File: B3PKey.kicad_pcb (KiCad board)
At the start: 2 copper layers, 178 parts, among them SW1 SW_Push, U1 ATmega32U4-AU, Y1 16MHz

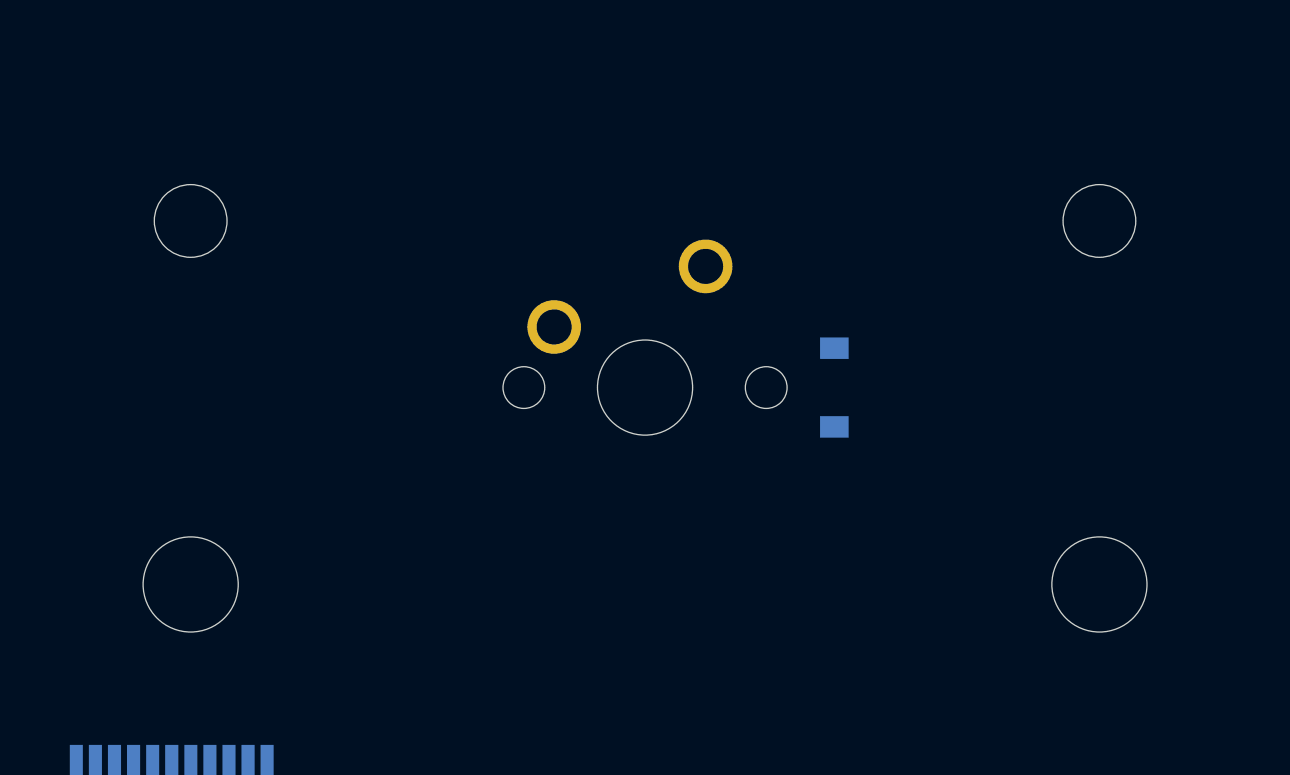
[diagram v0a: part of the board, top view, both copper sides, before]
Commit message: Flip spacebar stabs
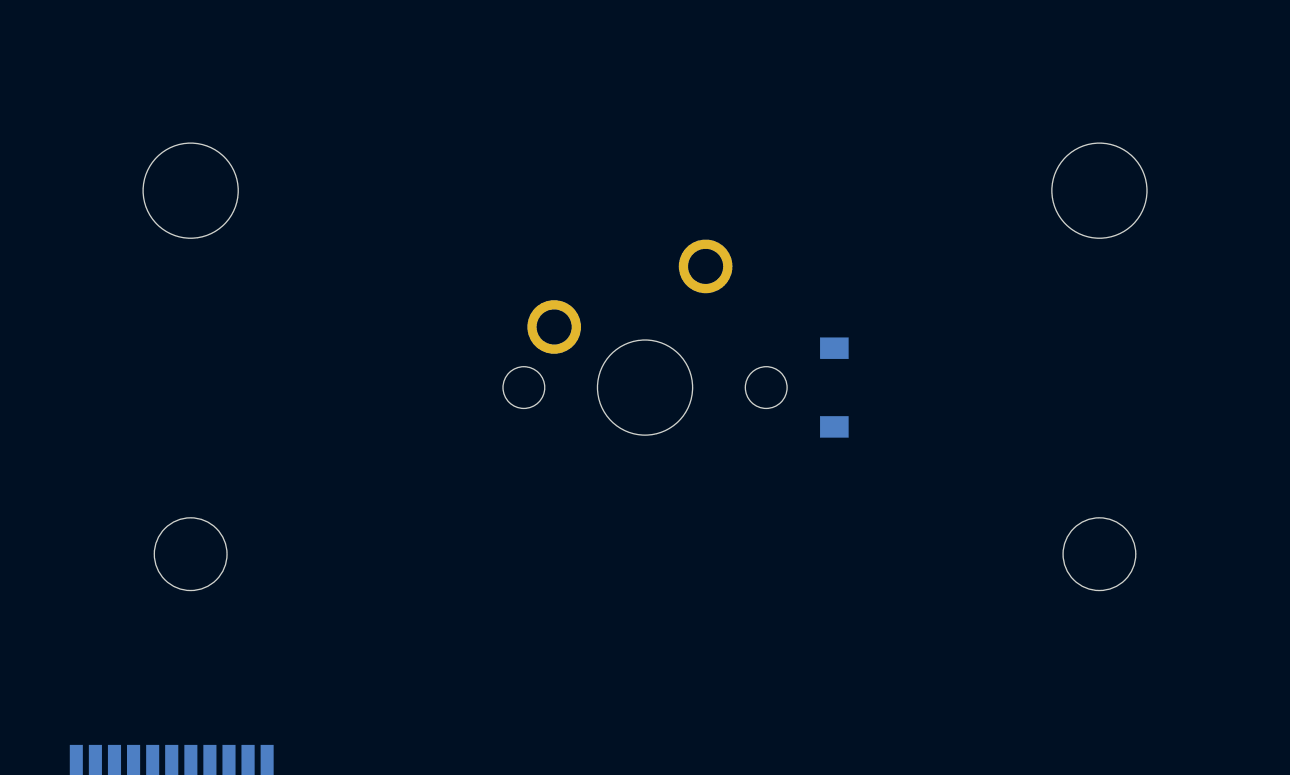
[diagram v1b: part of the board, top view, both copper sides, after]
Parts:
- MX74: footprint MX_Only:MXOnly-3U-NoLED -> MX_Only:MXOnly-3U-ReversedStabilizers-NoLED
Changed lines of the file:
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@@
     (add_net VCC)
+  )
+  (module MX_Only:MXOnly-3U-ReversedStabilizers-NoLED (layer F.Cu)
+    (at 117.475 117.475)
+    (fp_text reference MX74 (at 0 3.175) (layer Dwgs.User)
+      (effects (font (size 1 1) (thickness 0.15)))
+    )
+    (fp_text value MX-NoLED (at 0 -7.9375) (layer Dwgs.User)
+      (effects (font (size 1 1) (thickness 0.15)))
+    )
+    (fp_line (start 5 -7) (end 7 -7) (layer Dwgs.User) (width 0.15))
+    (fp_line (start 7 -7) (end 7 -5) (layer Dwgs.User) (width 0.15))
+    (fp_line (start 5 7) (end 7 7) (layer Dwgs.User) (width 0.15))
+    (fp_line (start 7 7) (end 7 5) (layer Dwgs.User) (width 0.15))
+    (fp_line (start -7 5) (end -7 7) (layer Dwgs.User) (width 0.15))
+    (fp_line (start -7 7) (end -5 7) (layer Dwgs.User) (width 0.15))
+    (fp_line (start -5 -7) (end -7 -7) (layer Dwgs.User) (width 0.15))
+    (fp_line (start -7 -7) (end -7 -5) (layer Dwgs.User) (width 0.15))
+    (fp_line (start -28.575 -9.525) (end 28.575 -9.525) (layer Dwgs.User) (width 0.15))
+    (fp_line (start 28.575 -9.525) (end 28.575 9.525) (layer Dwgs.User) (width 0.15))
+    (fp_line (start -28.575 9.525) (end 28.575 9.525) (layer Dwgs.User) (width 0.15))
+    (fp_line (start -28.575 9.525) (end -28.575 -9.525) (layer Dwgs.User) (width 0.15))
+    (pad 2 thru_hole circle (at 2.54 -5.08) (size 2.25 2.25) (drill 1.47) (layers *.Cu B.Mask)
+      (net 85 "Net-(D74-Pad2)"))
+    (pad 1 thru_hole circle (at -3.81 -2.54 48.1) (size 2.25 2.25) (drill 1.47) (layers *.Cu B.Mask)
+      (net 98 COL5))
+    (pad "" np_thru_hole circle (at 0 0) (size 3.9878 3.9878) (drill 3.9878) (layers *.Cu *.Mask))
+    (pad "" np_thru_hole circle (at -5.08 0 48.0996) (size 1.75 1.75) (drill 1.75) (layers *.Cu *.Mask))
+    (pad "" np_thru_hole circle (at 5.08 0 48.0996) (size 1.75 1.75) (drill 1.75) (layers *.Cu *.Mask))
+    (pad "" np_thru_hole circle (at -19.05 6.985) (size 3.048 3.048) (drill 3.048) (layers *.Cu *.Mask))
+    (pad "" np_thru_hole circle (at 19.05 6.985) (size 3.048 3.048) (drill 3.048) (layers *.Cu *.Mask))
+    (pad "" np_thru_hole circle (at -19.05 -8.255) (size 3.9878 3.9878) (drill 3.9878) (layers *.Cu *.Mask))
+    (pad "" np_thru_hole circle (at 19.05 -8.255) (size 3.9878 3.9878) (drill 3.9878) (layers *.Cu *.Mask))
   )
   (module MX_Only:MXOnly-1U-NoLED (layer F.Cu)
@@
     (pad "" np_thru_hole circle (at 5.08 0 48.0996) (size 1.75 1.75) (drill 1.75) (layers *.Cu *.Mask))
   )
-  (module MX_Only:MXOnly-3U-NoLED (layer F.Cu)
-    (at 117.475 117.475)
-    (fp_text reference MX74 (at 0 3.175) (layer Dwgs.User)
-      (effects (font (size 1 1) (thickness 0.15)))
-    )
-    (fp_text value MX-NoLED (at 0 -7.9375) (layer Dwgs.User)
-      (effects (font (size 1 1) (thickness 0.15)))
-    )
-    (fp_line (start 5 -7) (end 7 -7) (layer Dwgs.User) (width 0.15))
-    (fp_line (start 7 -7) (end 7 -5) (layer Dwgs.User) (width 0.15))
-    (fp_line (start 5 7) (end 7 7) (layer Dwgs.User) (width 0.15))
-    (fp_line (start 7 7) (end 7 5) (layer Dwgs.User) (width 0.15))
-    (fp_line (start -7 5) (end -7 7) (layer Dwgs.User) (width 0.15))
-    (fp_line (start -7 7) (end -5 7) (layer Dwgs.User) (width 0.15))
-    (fp_line (start -5 -7) (end -7 -7) (layer Dwgs.User) (width 0.15))
-    (fp_line (start -7 -7) (end -7 -5) (layer Dwgs.User) (width 0.15))
-    (fp_line (start -28.575 -9.525) (end 28.575 -9.525) (layer Dwgs.User) (width 0.15))
-    (fp_line (start 28.575 -9.525) (end 28.575 9.525) (layer Dwgs.User) (width 0.15))
-    (fp_line (start -28.575 9.525) (end 28.575 9.525) (layer Dwgs.User) (width 0.15))
-    (fp_line (start -28.575 9.525) (end -28.575 -9.525) (layer Dwgs.User) (width 0.15))
-    (pad 2 thru_hole circle (at 2.54 -5.08) (size 2.25 2.25) (drill 1.47) (layers *.Cu B.Mask)
-      (net 85 "Net-(D74-Pad2)"))
-    (pad 1 thru_hole circle (at -3.81 -2.54 48.1) (size 2.25 2.25) (drill 1.47) (layers *.Cu B.Mask)
-      (net 98 COL5))
-    (pad "" np_thru_hole circle (at 0 0) (size 3.9878 3.9878) (drill 3.9878) (layers *.Cu *.Mask))
-    (pad "" np_thru_hole circle (at -5.08 0 48.0996) (size 1.75 1.75) (drill 1.75) (layers *.Cu *.Mask))
-    (pad "" np_thru_hole circle (at 5.08 0 48.0996) (size 1.75 1.75) (drill 1.75) (layers *.Cu *.Mask))
-    (pad "" np_thru_hole circle (at -19.05 -6.985) (size 3.048 3.048) (drill 3.048) (layers *.Cu *.Mask))
-    (pad "" np_thru_hole circle (at 19.05 -6.985) (size 3.048 3.048) (drill 3.048) (layers *.Cu *.Mask))
-    (pad "" np_thru_hole circle (at -19.05 8.255) (size 3.9878 3.9878) (drill 3.9878) (layers *.Cu *.Mask))
-    (pad "" np_thru_hole circle (at 19.05 8.255) (size 3.9878 3.9878) (drill 3.9878) (layers *.Cu *.Mask))
-  )
-  (module MX_Only:MXOnly-1U-NoLED (layer F.Cu)
+  (module MX_Only:MXOnly-1U-NoLED (layer F.Cu)

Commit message: Matrix traces laid
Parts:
- moved D55 6.74 mm to (263.5, 84.1)
- moved D21 6.74 mm to (139.7, 46.0)
- moved D24 6.74 mm to (196.8, 46.0)
- moved D26 6.74 mm to (234.9, 46.0)
- moved D35 6.74 mm to (139.7, 65.1)
- moved D38 6.74 mm to (196.8, 65.1)
- moved D40 6.74 mm to (234.9, 65.1)
- moved D49 6.74 mm to (139.7, 84.1)
- moved D52 6.74 mm to (196.8, 84.1)
- moved D54 6.74 mm to (234.9, 84.1)
- moved D62 6.74 mm to (139.7, 103.2)
- moved D65 6.74 mm to (196.8, 103.2)
- moved D67 6.74 mm to (234.9, 103.2)
- moved D77 6.74 mm to (196.8, 122.2)
- moved D79 6.74 mm to (234.9, 122.2)
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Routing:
- net ROW5: track 0.00 -> 251.0 mm
- net ROW4: track 0.00 -> 247.7 mm
- net ROW2: track 0.00 -> 247.7 mm
- net ROW1: track 0.00 -> 247.7 mm
- net ROW0: track 0.00 -> 247.7 mm
- net ROW3: track 0.00 -> 239.0 mm
- net COL12: track 0.00 -> 105.3 mm
- net COL13: track 0.00 -> 96.3 mm
- net COL0: track 0.00 -> 95.3 mm
- net COL9: track 0.00 -> 95.2 mm
- net COL8: track 0.00 -> 95.2 mm
- net COL7: track 0.00 -> 95.2 mm
- net COL5: track 0.00 -> 95.2 mm
- net COL3: track 0.00 -> 95.2 mm
- net COL2: track 0.00 -> 95.2 mm
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
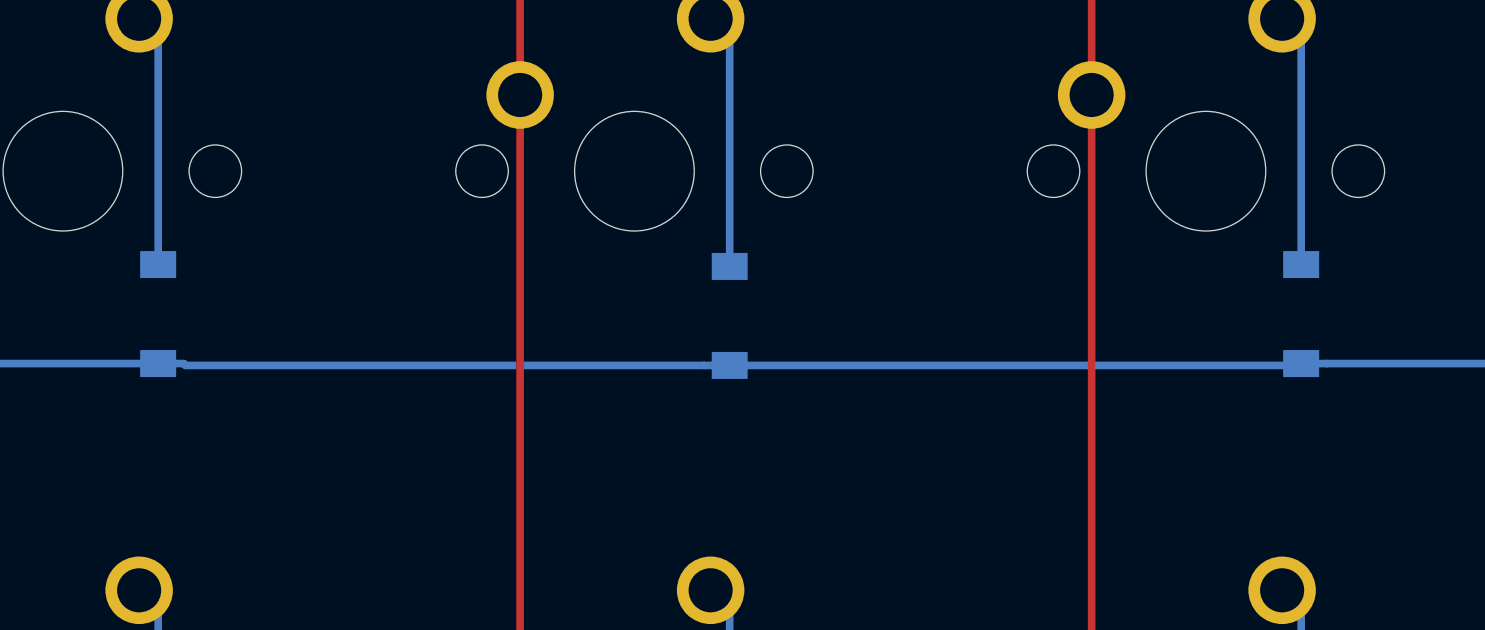
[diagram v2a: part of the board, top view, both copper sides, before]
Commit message: Matrix traces tweak
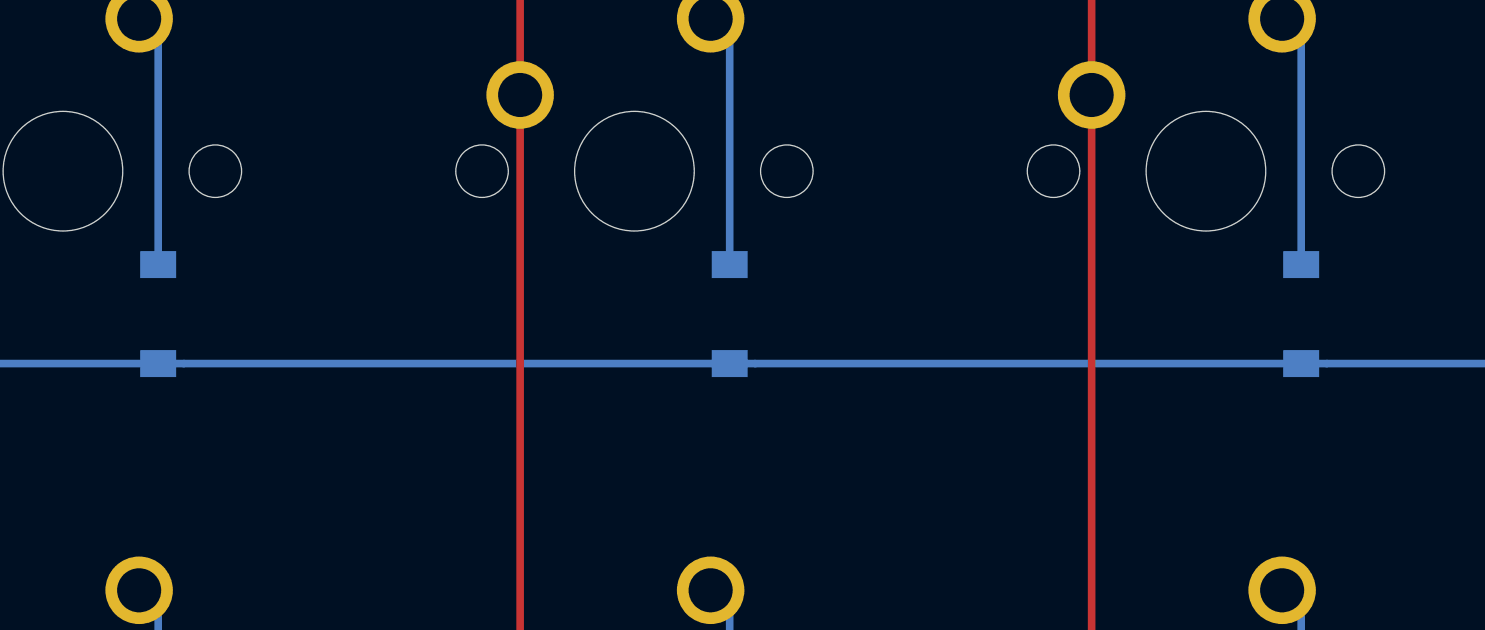
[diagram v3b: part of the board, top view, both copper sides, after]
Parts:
- moved D50 0.06 mm to (158.8, 84.1)
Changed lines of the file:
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@@
     (thickness 1.6)
     (drawings 0)
-    (tracks 366)
+    (tracks 365)
     (zones 0)
     (modules 178)
@@
   )
   (module Diode_SMD:D_SOD-123 (layer B.Cu)
-    (at 158.75 84.2 90)
+    (at 158.75 84.1375 90)
     (descr SOD-123)
     (tags SOD-123)
@@
   (segment (start 273.05 55.88) (end 272.415 55.245) (width 0.254) (layer B.Cu) (net 50))
   (segment (start 273.05 63.4375) (end 273.05 55.88) (width 0.254) (layer B.Cu) (net 50))
-  (segment (start 26.254 85.7875) (end 44.45 85.7875) (width 0.254) (layer B.Cu) (net 51))
-  (segment (start 25.4 85.7875) (end 26.254 85.7875) (width 0.254) (layer B.Cu) (net 51))
-  (segment (start 45.304 85.7875) (end 63.5 85.7875) (width 0.254) (layer B.Cu) (net 51))
-  (segment (start 44.45 85.7875) (end 45.304 85.7875) (width 0.254) (layer B.Cu) (net 51))
-  (segment (start 64.354 85.7875) (end 82.55 85.7875) (width 0.254) (layer B.Cu) (net 51))
-  (segment (start 63.5 85.7875) (end 64.354 85.7875) (width 0.254) (layer B.Cu) (net 51))
-  (segment (start 83.404 85.7875) (end 101.6 85.7875) (width 0.254) (layer B.Cu) (net 51))
-  (segment (start 82.55 85.7875) (end 83.404 85.7875) (width 0.254) (layer B.Cu) (net 51))
-  (segment (start 102.454 85.7875) (end 120.65 85.7875) (width 0.254) (layer B.Cu) (net 51))
-  (segment (start 101.6 85.7875) (end 102.454 85.7875) (width 0.254) (layer B.Cu) (net 51))
-  (segment (start 121.504 85.7875) (end 139.7 85.7875) (width 0.254) (layer B.Cu) (net 51))
-  (segment (start 120.65 85.7875) (end 121.504 85.7875) (width 0.254) (layer B.Cu) (net 51))
-  (segment (start 157.896 85.85) (end 158.75 85.85) (width 0.254) (layer B.Cu) (net 51))
-  (segment (start 140.6165 85.85) (end 157.896 85.85) (width 0.254) (layer B.Cu) (net 51))
-  (segment (start 140.554 85.7875) (end 140.6165 85.85) (width 0.254) (layer B.Cu) (net 51))
-  (segment (start 139.7 85.7875) (end 140.554 85.7875) (width 0.254) (layer B.Cu) (net 51))
   (segment (start 177.7375 85.85) (end 177.8 85.7875) (width 0.254) (layer B.Cu) (net 51))
-  (segment (start 158.75 85.85) (end 177.7375 85.85) (width 0.254) (layer B.Cu) (net 51))
   (segment (start 178.654 85.7875) (end 196.85 85.7875) (width 0.254) (layer B.Cu) (net 51))
   (segment (start 177.8 85.7875) (end 178.654 85.7875) (width 0.254) (layer B.Cu) (net 51))
@@
   (segment (start 236.7555 84.836) (end 235.804 85.7875) (width 0.254) (layer B.Cu) (net 51))
   (segment (start 261.7195 84.836) (end 236.7555 84.836) (width 0.254) (layer B.Cu) (net 51))
+  (segment (start 120.65 85.7875) (end 121.504 85.7875) (width 0.254) (layer B.Cu) (net 51))
+  (segment (start 102.454 85.7875) (end 120.65 85.7875) (width 0.254) (layer B.Cu) (net 51))
+  (segment (start 63.5 85.7875) (end 64.354 85.7875) (width 0.254) (layer B.Cu) (net 51))
+  (segment (start 64.354 85.7875) (end 82.55 85.7875) (width 0.254) (layer B.Cu) (net 51))
+  (segment (start 26.254 85.7875) (end 44.45 85.7875) (width 0.254) (layer B.Cu) (net 51))
+  (segment (start 44.45 85.7875) (end 45.304 85.7875) (width 0.254) (layer B.Cu) (net 51))
+  (segment (start 25.4 85.7875) (end 26.254 85.7875) (width 0.254) (layer B.Cu) (net 51))
+  (segment (start 121.504 85.7875) (end 139.7 85.7875) (width 0.254) (layer B.Cu) (net 51))
+  (segment (start 82.55 85.7875) (end 83.404 85.7875) (width 0.254) (layer B.Cu) (net 51))
+  (segment (start 83.404 85.7875) (end 101.6 85.7875) (width 0.254) (layer B.Cu) (net 51))
+  (segment (start 101.6 85.7875) (end 102.454 85.7875) (width 0.254) (layer B.Cu) (net 51))
+  (segment (start 45.304 85.7875) (end 63.5 85.7875) (width 0.254) (layer B.Cu) (net 51))
+  (segment (start 140.554 85.7875) (end 158.75 85.7875) (width 0.254) (layer B.Cu) (net 51))
+  (segment (start 139.7 85.7875) (end 140.554 85.7875) (width 0.254) (layer B.Cu) (net 51))
+  (segment (start 159.604 85.7875) (end 177.8 85.7875) (width 0.254) (layer B.Cu) (net 51))
+  (segment (start 158.75 85.7875) (end 159.604 85.7875) (width 0.254) (layer B.Cu) (net 51))
   (segment (start 25.4 74.93) (end 24.765 74.295) (width 0.254) (layer B.Cu) (net 52))
   (segment (start 25.4 82.4875) (end 25.4 74.93) (width 0.254) (layer B.Cu) (net 52))

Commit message: Add Elite-C footprint
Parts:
- added U1: Elite-C, Keebio-Parts:Elite-C, F.Cu at (60.3, 30.7)
- moved D17 3.24 mm to (63.5, 49.3)
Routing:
- net Net-(D17-Pad2): track 8.46 -> 13.1 mm
- net ROW1: track 247.7 -> 250.3 mm
- net ROW0: track 247.7 -> 248.3 mm

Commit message: Update layout and replace microcontroller
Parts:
- removed C1, C2: 22pF, Capacitor_SMD:C_0805_2012Metric
- removed C3: 1uF, Capacitor_SMD:C_0805_2012Metric
- removed C4, C5, C6: 0.1uF, Capacitor_SMD:C_0805_2012Metric
- removed C7: 10uF, Capacitor_SMD:C_0805_2012Metric
- removed F1: 500mA, Fuse:Fuse_0805_2012Metric
- removed R1, R4: 10k, Resistor_SMD:R_0805_2012Metric
- removed R2, R3: 22, Resistor_SMD:R_0805_2012Metric
- removed SW1: SW_Push, random-keyboard-parts:SKQG-1155865
- removed U1: ATmega32U4-AU, Package_QFP:TQFP-44_10x10mm_P0.8mm
- removed U1: Elite-C, Keebio-Parts:Elite-C
- removed USB1: Molex-0548190589, random-keyboard-parts:Molex-0548190589
- removed Y1: 16MHz, Crystal:Crystal_SMD_3225-4Pin_3.2x2.5mm
- added U2: Elite-C, Keebio-Parts:Elite-C, F.Cu at (60.3, 30.7)
- MX74: footprint MX_Only:MXOnly-3U-ReversedStabilizers-NoLED -> MX_Only:MXOnly-2U-ReversedStabilizers-NoLED
- MX75: footprint MX_Only:MXOnly-1U-NoLED -> MX_Only:MXOnly-2U-ReversedStabilizers-NoLED
- moved D74 9.53 mm to (111.1, 122.2)
- moved D75 9.53 mm to (149.2, 122.2)
- moved MX74 9.52 mm to (108.0, 117.5)
- moved MX75 9.52 mm to (146.1, 117.5)
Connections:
- MX75 pad 1: COL7 -> COL6
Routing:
- net COL6: track 76.2 -> 99.2 mm
- net COL5: track 95.2 -> 99.2 mm

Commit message: Modify silkscreen
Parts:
- U2: value Elite-C -> Elite-C-mod; footprint Keebio-Parts:Elite-C -> Keebio-Parts:Elite-C-mod
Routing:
- net COL7: track 95.2 -> 76.2 mm
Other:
- board outline added: 270.8 x 118.4 mm
